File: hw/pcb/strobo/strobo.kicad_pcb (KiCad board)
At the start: 2 copper layers, 74 x 74 mm, 92 parts, among them J1 Conn_ARM_JTAG_SWD_10, SW1 SW_SPST, U1 ICM-20602, U2 STM32L051K8Ux, U3 Ring_Tracks, Y1 32kHz

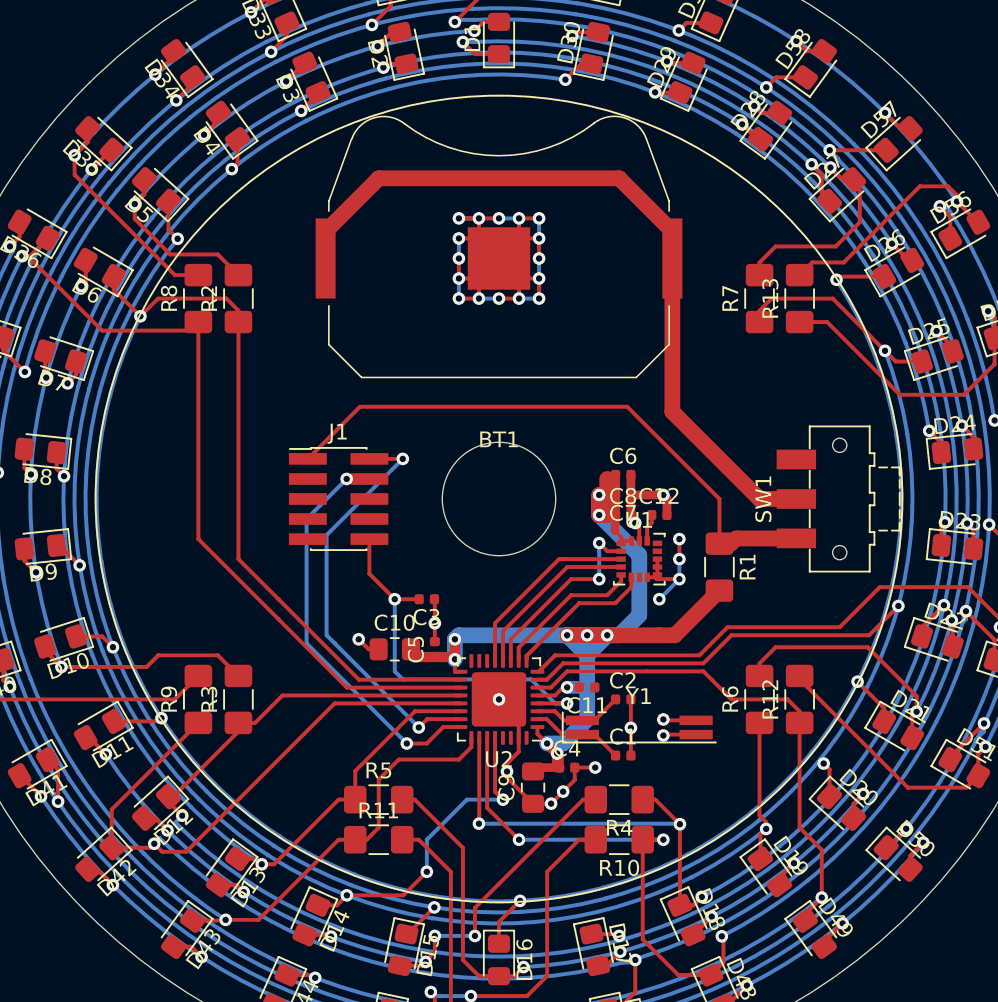
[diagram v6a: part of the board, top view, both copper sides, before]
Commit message: cosmetics, ref placement etc
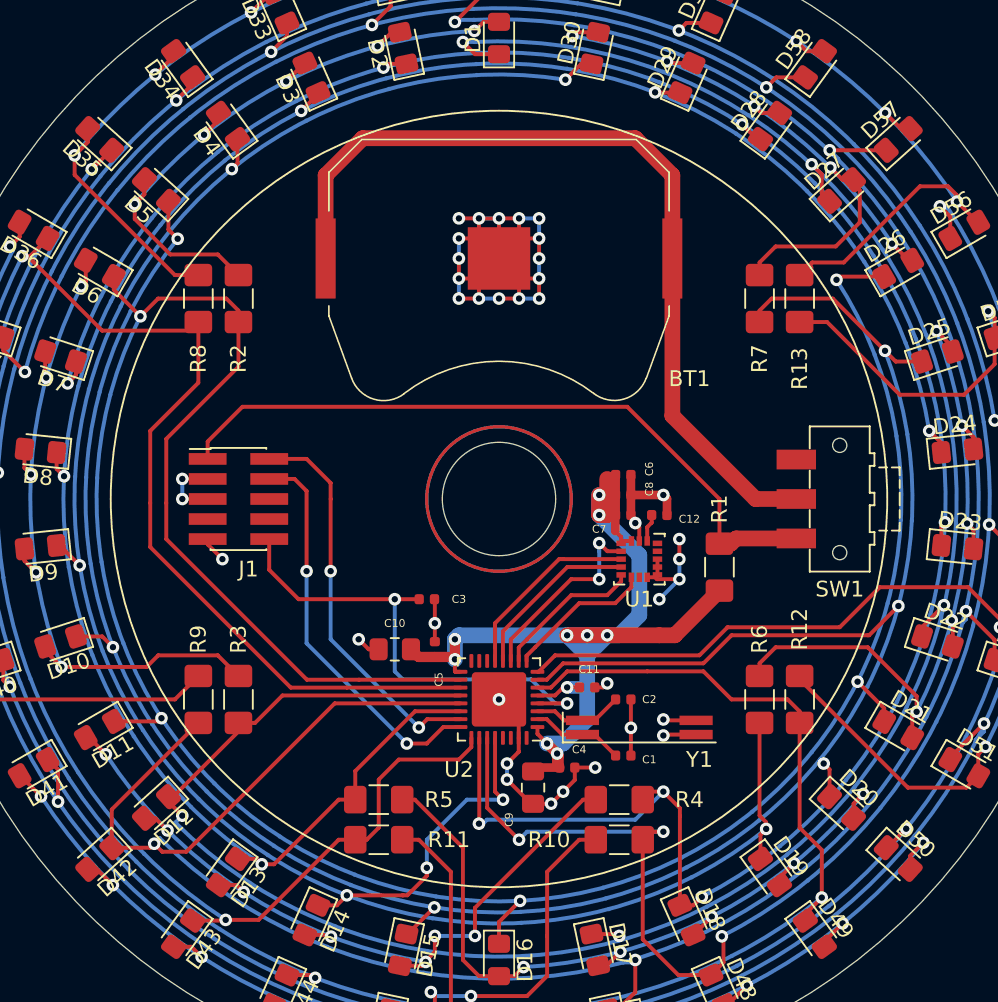
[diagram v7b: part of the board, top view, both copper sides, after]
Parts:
- moved J1 6.35 mm to (184.2, 100.3)
- turned BT1 to 0 degrees
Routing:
- net GND: track 90.4 -> 98.8 mm, vias 32 -> 37
- net VDD: track 37.7 -> 44.7 mm
- net Net-(BT1-Pad1): track 48.0 -> 54.5 mm
- net NRST: track 24.2 -> 30.4 mm
- net RA: track 55.9 -> 61.6 mm
- net SA: track 64.9 -> 69.5 mm
- net Net-(C10-Pad2): track 70.2 -> 71.2 mm
- net SWDIO: track 26.4 -> 25.4 mm
- net RC: track 34.6 -> 35.4 mm
- net SWCLK: track 25.7 -> 25.2 mm
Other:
- board text added: "Jonas A 2019"
- board text added: "REV A1"

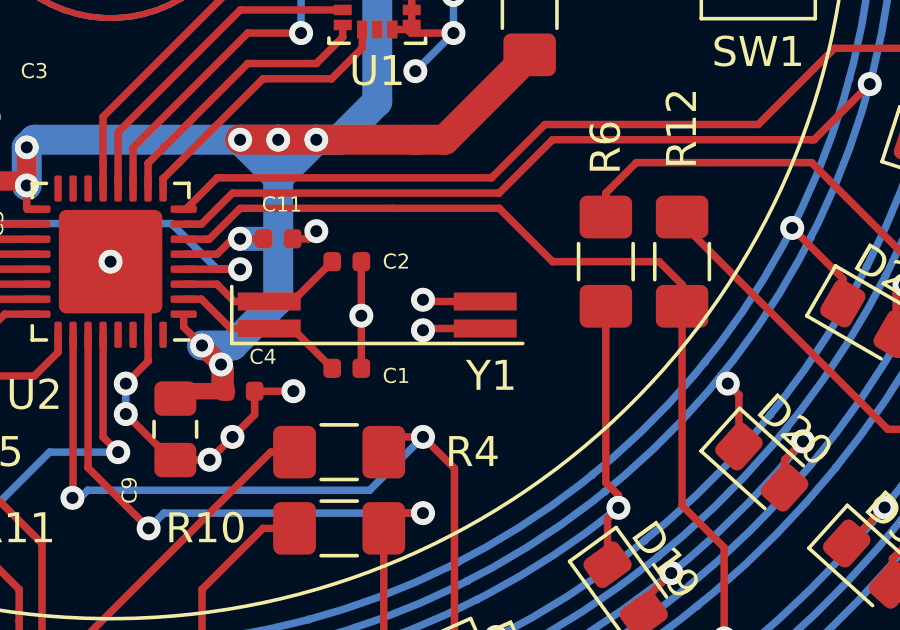
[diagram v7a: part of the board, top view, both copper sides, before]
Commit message: pin 2 and 3 of oscillator should be nc...
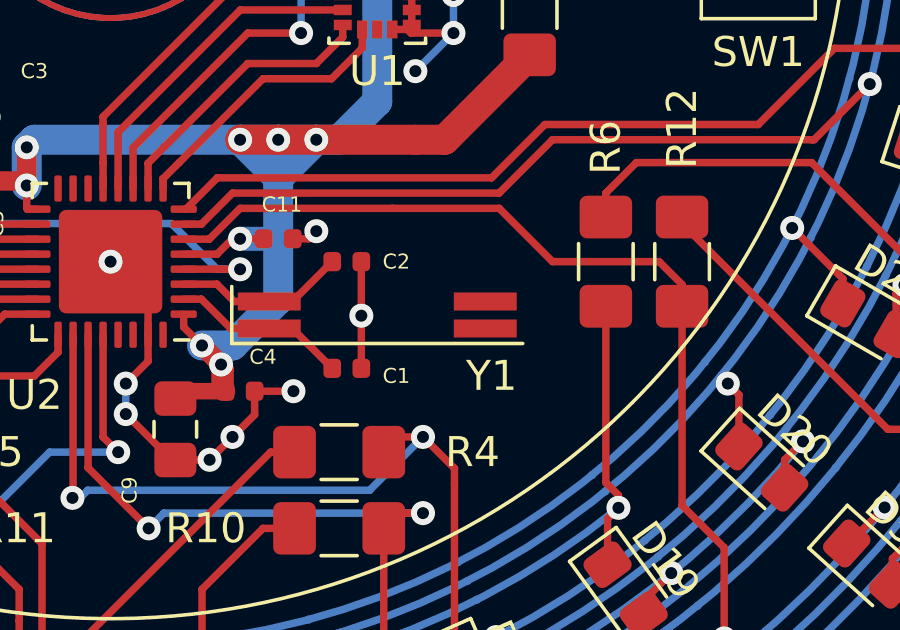
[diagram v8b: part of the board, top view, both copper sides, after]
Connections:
- Y1 pad 2: GND -> Net-(Y1-Pad2)
- Y1 pad 3: GND -> Net-(Y1-Pad3)
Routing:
- net GND: track 98.8 -> 94.6 mm, vias 37 -> 35
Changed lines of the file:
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@@
     (thickness 1.6)
     (drawings 11)
-    (tracks 890)
+    (tracks 882)
     (zones 0)
     (modules 92)
-    (nets 50)
+    (nets 52)
   )
   (page A4)
@@
   (net 48 "Net-(U2-Pad30)")
   (net 49 "Net-(U2-Pad29)")
+  (net 50 "Net-(Y1-Pad3)")
+  (net 51 "Net-(Y1-Pad2)")
   (net_class Default "This is the default net class."
     (clearance 0.1524)
@@
     (add_net "Net-(U2-Pad30)")
     (add_net "Net-(U2-Pad32)")
+    (add_net "Net-(Y1-Pad2)")
+    (add_net "Net-(Y1-Pad3)")
     (add_net RA)
     (add_net RB)
@@
       (net 4 "Net-(C2-Pad1)"))
     (pad 3 smd rect (at 3.6 -0.45) (size 2.1 0.6) (layers F.Cu F.Paste F.Mask)
-      (net 1 GND))
+      (net 50 "Net-(Y1-Pad3)"))
     (pad 2 smd rect (at 3.6 0.45) (size 2.1 0.6) (layers F.Cu F.Paste F.Mask)
-      (net 1 GND))
+      (net 51 "Net-(Y1-Pad2)"))
     (pad 1 smd rect (at -3.6 0.45) (size 2.1 0.6) (layers F.Cu F.Paste F.Mask)
       (net 3 "Net-(C1-Pad1)"))
@@
   (segment (start 205.463 117.348) (end 206.756 117.348) (width 0.25) (layer F.Cu) (net 1) (status 400000))
   (segment (start 209.019 113.03) (end 209.019 114.831) (width 0.25) (layer F.Cu) (net 1) (status C00000))
-  (segment (start 213.15 114.358) (end 211.132 114.358) (width 0.25) (layer F.Cu) (net 1) (status 400000))
-  (segment (start 211.132 114.358) (end 211.074 114.3) (width 0.25) (layer F.Cu) (net 1))
-  (segment (start 213.15 115.258) (end 211.132 115.258) (width 0.25) (layer F.Cu) (net 1) (status 400000))
-  (segment (start 211.132 115.258) (end 211.074 115.316) (width 0.25) (layer F.Cu) (net 1))
   (segment (start 206.756 117.348) (end 206.756 117.348) (width 0.25) (layer F.Cu) (net 1) (status 400000))
   (via (at 206.756 117.348) (size 0.8) (drill 0.4) (layers F.Cu B.Cu) (net 1))
   (segment (start 209.019 114.831) (end 209.019 116.586) (width 0.25) (layer F.Cu) (net 1) (status C00000))
   (via (at 209.019 114.831) (size 0.8) (drill 0.4) (layers F.Cu B.Cu) (net 1))
-  (segment (start 211.074 114.3) (end 211.074 114.3) (width 0.25) (layer F.Cu) (net 1))
-  (via (at 211.074 114.3) (size 0.8) (drill 0.4) (layers F.Cu B.Cu) (net 1))
-  (segment (start 211.074 115.316) (end 211.074 115.316) (width 0.25) (layer F.Cu) (net 1))
-  (via (at 211.074 115.316) (size 0.8) (drill 0.4) (layers F.Cu B.Cu) (net 1))
   (segment (start 193.031 109.855) (end 192.405 109.855) (width 0.25) (layer F.Cu) (net 1) (status 400000))
   (via (at 191.77 109.22) (size 0.8) (drill 0.4) (layers F.Cu B.Cu) (net 1))
